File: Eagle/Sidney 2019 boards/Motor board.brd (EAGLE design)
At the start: 110 x 122 mm, 43 parts, among them IC2 LM2940CS-5.0_NOPB, IC3 LM3940IS-3.3

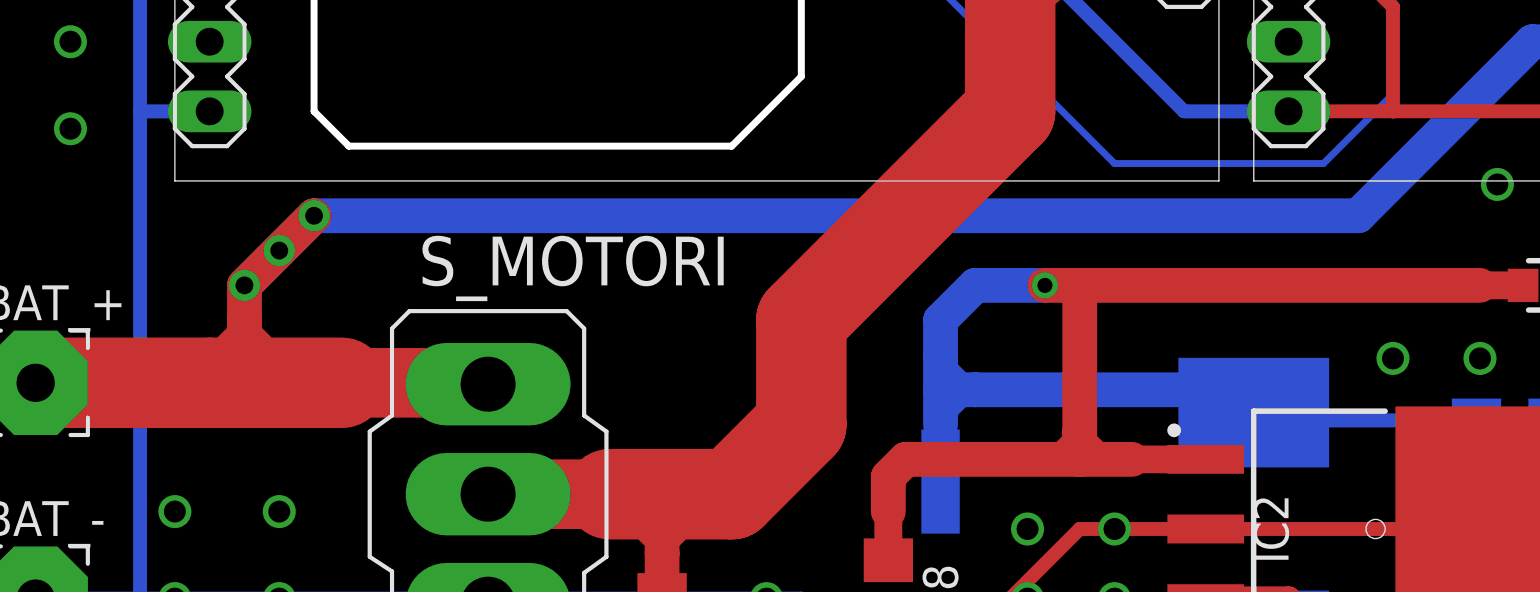
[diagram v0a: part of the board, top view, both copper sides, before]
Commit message: Fixed thin ground trace near battery power
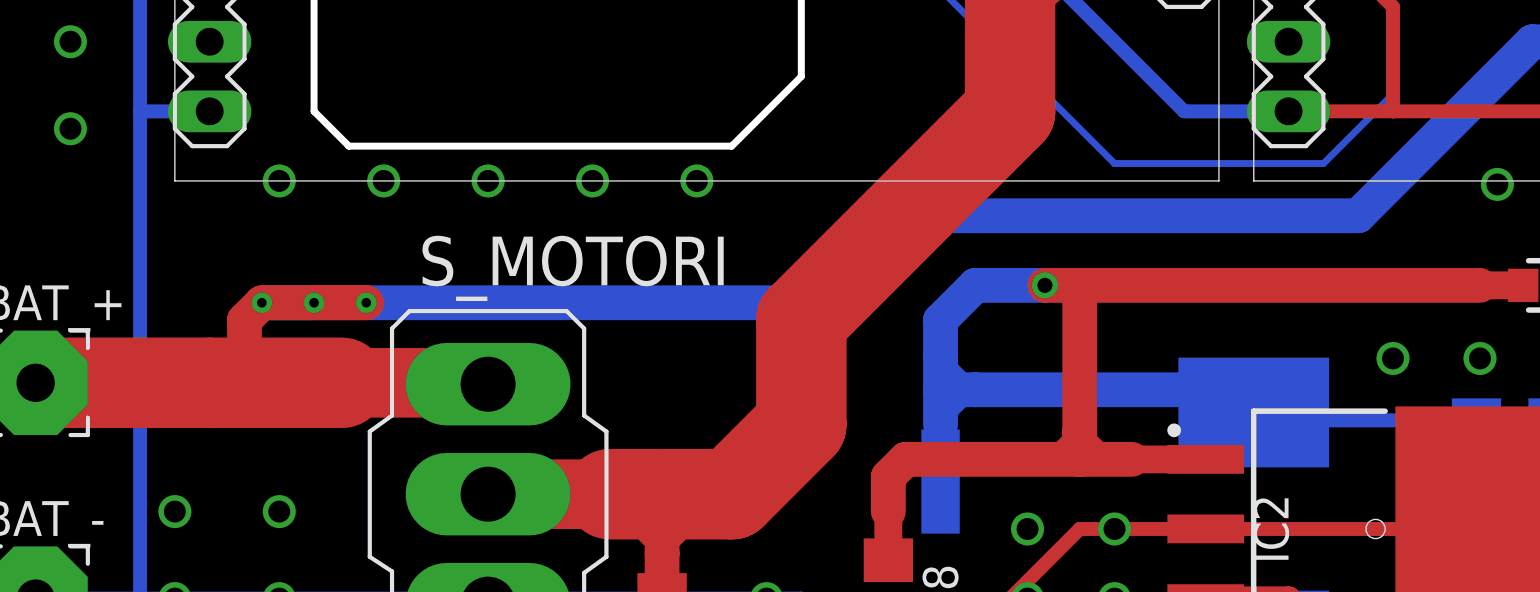
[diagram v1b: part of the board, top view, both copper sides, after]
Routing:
- net N$1: track 117.8 -> 115.8 mm
- net GND: vias 73 -> 78
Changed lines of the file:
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@@
 <via x="126.365" y="85.725" extent="1-16" drill="0.8"/>
 <via x="128.905" y="88.265" extent="1-16" drill="0.8"/>
+<via x="60.96" y="73.66" extent="1-16" drill="0.8"/>
+<via x="57.15" y="73.66" extent="1-16" drill="0.8"/>
+<via x="53.34" y="73.66" extent="1-16" drill="0.8"/>
+<via x="49.53" y="73.66" extent="1-16" drill="0.8"/>
+<via x="45.72" y="73.66" extent="1-16" drill="0.8"/>
 </signal>
 <signal name="+5V">
@@
 <contactref element="BAT_+" pad="1"/>
 <wire x1="36.83" y1="66.294" x2="43.18" y2="66.294" width="3.302" layer="1"/>
-<wire x1="43.18" y1="66.294" x2="44.45" y2="66.294" width="3.302" layer="1"/>
-<wire x1="44.45" y1="66.294" x2="48.006" y2="66.294" width="3.302" layer="1"/>
+<wire x1="43.18" y1="66.294" x2="48.006" y2="66.294" width="3.302" layer="1"/>
 <wire x1="48.006" y1="66.294" x2="53.2892" y2="66.294" width="2.54" layer="1"/>
 <wire x1="53.2892" y1="66.294" x2="53.34" y2="66.2432" width="2.54" layer="1"/>
 <wire x1="91.44" y1="78.74" x2="85.09" y2="72.39" width="1.27" layer="16"/>
-<wire x1="85.09" y1="72.39" x2="46.99" y2="72.39" width="1.27" layer="16"/>
-<wire x1="46.99" y1="72.39" x2="45.72" y2="71.12" width="1.27" layer="16"/>
-<via x="44.45" y="69.85" extent="1-16" drill="0.65" diameter="1.15"/>
-<wire x1="45.72" y1="71.12" x2="44.45" y2="69.85" width="1.27" layer="16"/>
-<wire x1="44.45" y1="66.294" x2="44.45" y2="68.58" width="1.27" layer="1"/>
-<wire x1="44.45" y1="69.85" x2="44.45" y2="68.58" width="1.27" layer="1"/>
-<wire x1="44.45" y1="69.85" x2="45.72" y2="71.12" width="1.27" layer="1"/>
-<via x="46.99" y="72.39" extent="1-16" drill="0.65" diameter="1.15"/>
-<wire x1="45.72" y1="71.12" x2="46.99" y2="72.39" width="1.27" layer="1"/>
-<via x="45.72" y="71.12" extent="1-16" drill="0.65" diameter="1.15"/>
-<wire x1="43.18" y1="66.294" x2="43.18" y2="67.31" width="0.508" layer="1"/>
-<wire x1="43.18" y1="67.31" x2="44.45" y2="68.58" width="0.508" layer="1"/>
-<wire x1="44.45" y1="68.58" x2="45.212" y2="67.818" width="0.508" layer="1"/>
+<wire x1="43.18" y1="66.294" x2="44.45" y2="67.564" width="1.27" layer="1"/>
+<wire x1="44.45" y1="67.564" x2="44.45" y2="68.58" width="1.27" layer="1"/>
+<wire x1="44.45" y1="68.58" x2="45.085" y2="69.215" width="1.27" layer="1"/>
+<wire x1="69.215" y1="72.39" x2="66.04" y2="69.215" width="1.27" layer="16"/>
+<wire x1="66.04" y1="69.215" x2="45.085" y2="69.215" width="1.27" layer="16"/>
+<wire x1="85.09" y1="72.39" x2="69.215" y2="72.39" width="1.27" layer="16"/>
+<via x="45.085" y="69.215" extent="1-16" drill="0.35"/>
+<wire x1="45.085" y1="69.215" x2="48.895" y2="69.215" width="1.27" layer="1"/>
+<via x="46.99" y="69.215" extent="1-16" drill="0.35"/>
+<via x="48.895" y="69.215" extent="1-16" drill="0.35"/>
+<wire x1="46.99" y1="69.215" x2="48.895" y2="69.215" width="1.27" layer="1"/>
 </signal>
 <signal name="VCC">

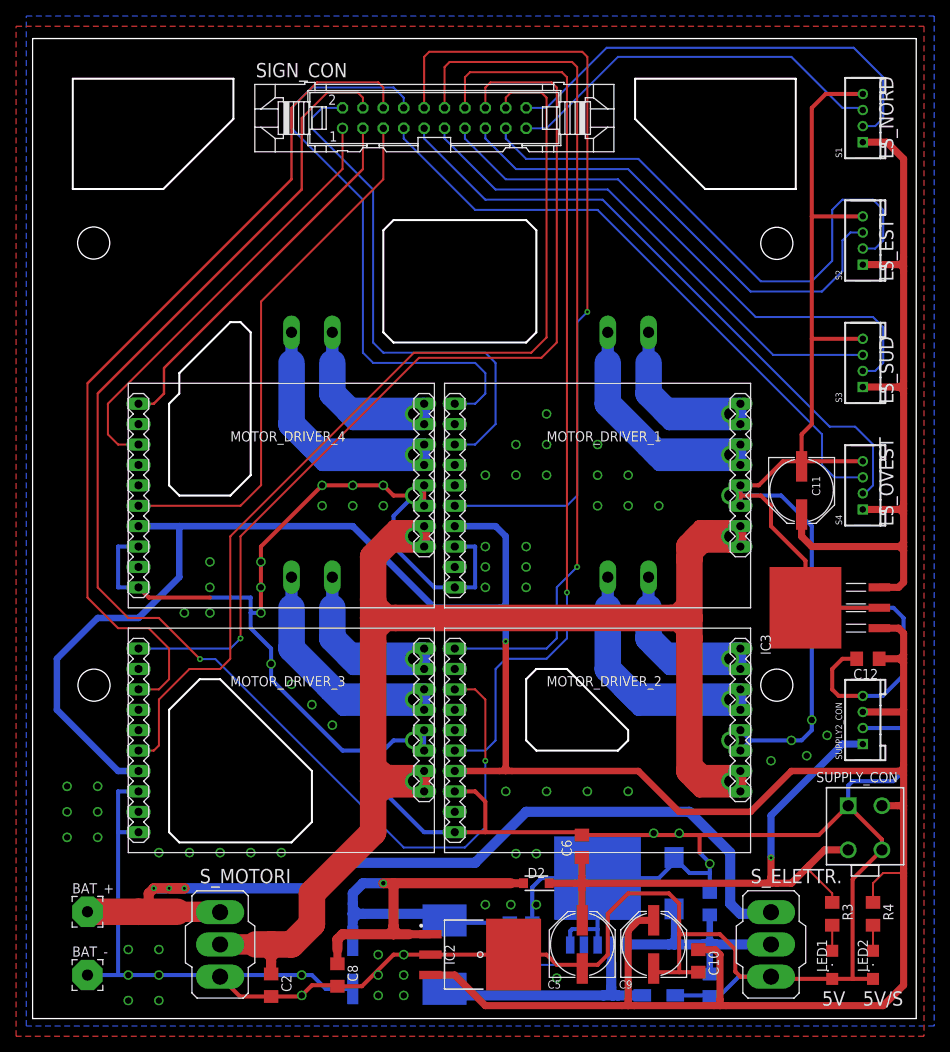
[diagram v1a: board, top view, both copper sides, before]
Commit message: Created line sensors layout for gerber generation. Added logos to uC and motor PCBs. Generater and uploaded on PCBWAY every gerber
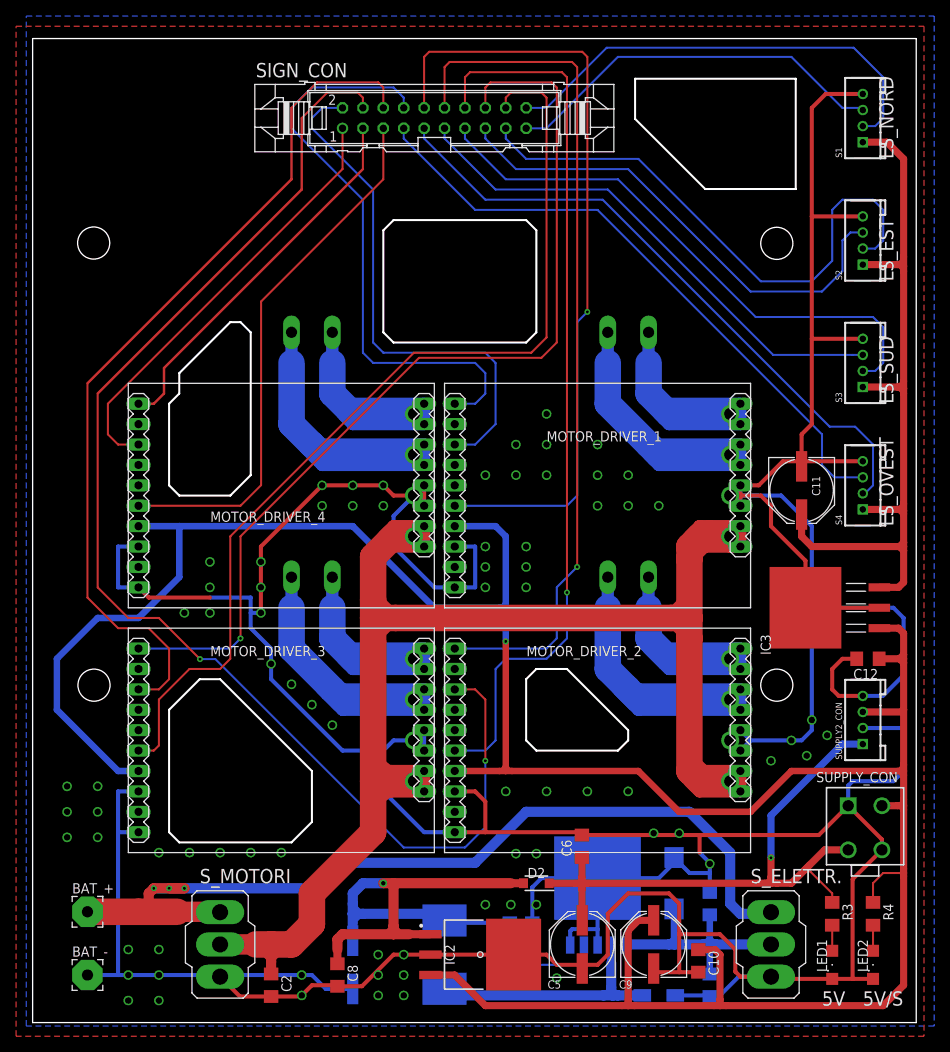
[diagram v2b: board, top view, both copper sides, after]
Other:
- board size 110 x 122 mm -> 110 x 122.5 mm
